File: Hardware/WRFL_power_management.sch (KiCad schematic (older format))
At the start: 38 parts, among them P1 JST_XH_2, P2 TEST_POINT, P3 TEST_POINT, P4 JST_XH_2, P5 TEST_POINT, P6 TEST_POINT, P7 TEST_POINT, Q1 SI1012CR, Q2 SI2333DDS, U1 TPS73633DCQ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

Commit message: Added VREF and 2x3 for servos
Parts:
- R6: value 100k -> 1M
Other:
- moved on the sheet: C6, C7, C8, C9, D2, L1, P7, R8, R9, U4

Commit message: Added VBAT sens
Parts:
- added P17: 1x2_2_54_MALE, symbol CONN_2
- added Q4: SI1012CR, SC-75A, symbol SI1012CR
- added R19, R20: 9.09k_0.1%, ~, symbol R
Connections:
- net labels added: MEAS_EN, VBAT_SENS
- wire segments 96 -> 105
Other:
- note added: "Power on switch + User switch\nUsing the rotary encoder's push button"
- moved on the sheet: R14, R15
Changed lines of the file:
@@
-EESchema Schematic File Version 2  date 10/7/2013 7:37:21 AM
+EESchema Schematic File Version 2  date Monday, October 07, 2013 09:14:17 AM
 LIBS:power
 LIBS:device
@@
 Wire Wire Line
 	6200 1900 6200 2050
-Wire Wire Line
-	6200 2050 7250 2050
-Connection ~ 6750 2050
-$Comp
-L GND #PWR21
+$Comp
+L GND #PWR22
 U 1 1 524B2F1B
 P 6750 3650
-F 0 "#PWR21" H 6750 3650 30  0001 C CNN
+F 0 "#PWR22" H 6750 3650 30  0001 C CNN
 F 1 "GND" H 6750 3580 30  0001 C CNN
 F 2 "" H 6750 3650 60  0000 C CNN
@@
 $EndComp
 $Comp
-L GND #PWR19
+L GND #PWR20
 U 1 1 524B2F2A
 P 6050 3650
-F 0 "#PWR19" H 6050 3650 30  0001 C CNN
+F 0 "#PWR20" H 6050 3650 30  0001 C CNN
 F 1 "GND" H 6050 3580 30  0001 C CNN
 F 2 "" H 6050 3650 60  0000 C CNN
@@
 	3600 6600 3600 6800
 Wire Wire Line
-	3200 6450 4700 6450
+	3200 6450 5400 6450
 Wire Wire Line
 	4150 6450 4150 6800
@@
 Wire Wire Line
 	6950 1300 7700 1300
-Text GLabel 10500 2050 2    60   Input ~ 0
+Text GLabel 10550 3550 2    60   Input ~ 0
 PM_ENABLE
 Wire Wire Line
-	9400 2050 10500 2050
-Text Label 9950 2050 0    60   ~ 0
+	9650 3550 10550 3550
+Text Label 10000 3550 0    60   ~ 0
 PM_EN
 $Comp
@@
 	8550 5950 8550 6000
 $Comp
-L GND #PWR22
+L GND #PWR23
 U 1 1 5251B5EF
 P 8550 6000
-F 0 "#PWR22" H 8550 6000 30  0001 C CNN
+F 0 "#PWR23" H 8550 6000 30  0001 C CNN
 F 1 "GND" H 8550 5930 30  0001 C CNN
 F 2 "" H 8550 6000 60  0000 C CNN
@@
 $EndComp
 $Comp
-L GND #PWR20
+L GND #PWR21
 U 1 1 5251B5FE
 P 6650 5900
-F 0 "#PWR20" H 6650 5900 30  0001 C CNN
+F 0 "#PWR21" H 6650 5900 30  0001 C CNN
 F 1 "GND" H 6650 5830 30  0001 C CNN
 F 2 "" H 6650 5900 60  0000 C CNN
@@
 $EndComp
 $Comp
-L GND #PWR25
+L GND #PWR26
 U 1 1 5251B60D
 P 10050 6150
-F 0 "#PWR25" H 10050 6150 30  0001 C CNN
+F 0 "#PWR26" H 10050 6150 30  0001 C CNN
 F 1 "GND" H 10050 6080 30  0001 C CNN
 F 2 "" H 10050 6150 60  0000 C CNN
@@
 $EndComp
 $Comp
-L GND #PWR23
+L GND #PWR24
 U 1 1 5251B61C
 P 9250 6900
-F 0 "#PWR23" H 9250 6900 30  0001 C CNN
+F 0 "#PWR24" H 9250 6900 30  0001 C CNN
 F 1 "GND" H 9250 6830 30  0001 C CNN
 F 2 "" H 9250 6900 60  0000 C CNN
@@
 	7300 6150 6500 6150
 $Comp
-L V_BOOST #U9
+L V_BOOST #U10
 U 1 1 5251BF9B
 P 10550 5000
-F 0 "#U9" H 10550 5200 60  0001 C CNN
+F 0 "#U10" H 10550 5200 60  0001 C CNN
 F 1 "V_BOOST" H 10550 5100 60  0000 C CNN
 F 2 "~" H 10550 5000 60  0000 C CNN
@@
 $EndComp
 $Comp
-L GND #PWR18
+L GND #PWR19
 U 1 1 5251E6D3
 P 5700 2000
-F 0 "#PWR18" H 5700 2000 30  0001 C CNN
+F 0 "#PWR19" H 5700 2000 30  0001 C CNN
 F 1 "GND" H 5700 1930 30  0001 C CNN
 F 2 "" H 5700 2000 60  0000 C CNN
@@
 Wire Wire Line
 	5700 1800 5700 2000
-Text GLabel 7250 2050 2    60   Input ~ 0
+Text GLabel 7450 3550 2    60   Input ~ 0
 ON_SW_FET
 $Comp
 L R R15
 U 1 1 52521245
-P 9800 2450
-F 0 "R15" V 9880 2450 40  0000 C CNN
-F 1 "100k" V 9807 2451 40  0000 C CNN
-F 2 "~" V 9730 2450 30  0000 C CNN
-F 3 "~" H 9800 2450 30  0000 C CNN
-	1    9800 2450
-	1    0    0    -1
-$EndComp
-$Comp
-L GND #PWR24
+P 9850 3950
+F 0 "R15" V 9930 3950 40  0000 C CNN
+F 1 "100k" V 9857 3951 40  0000 C CNN
+F 2 "~" V 9780 3950 30  0000 C CNN
+F 3 "~" H 9850 3950 30  0000 C CNN
+	1    9850 3950
+	1    0    0    -1
+$EndComp
+$Comp
+L GND #PWR25
 U 1 1 5252124B
-P 9800 2900
-F 0 "#PWR24" H 9800 2900 30  0001 C CNN
-F 1 "GND" H 9800 2830 30  0001 C CNN
-F 2 "" H 9800 2900 60  0000 C CNN
-F 3 "" H 9800 2900 60  0000 C CNN
-	1    9800 2900
-	1    0    0    -1
-$EndComp
-Wire Wire Line
-	9800 2200 9800 2050
-Connection ~ 9800 2050
-Wire Wire Line
-	9800 2700 9800 2900
+P 9850 4400
+F 0 "#PWR25" H 9850 4400 30  0001 C CNN
+F 1 "GND" H 9850 4330 30  0001 C CNN
+F 2 "" H 9850 4400 60  0000 C CNN
+F 3 "" H 9850 4400 60  0000 C CNN
+	1    9850 4400
+	1    0    0    -1
+$EndComp
+Wire Wire Line
+	9850 3700 9850 3550
+Connection ~ 9850 3550
+Wire Wire Line
+	9850 4200 9850 4400
 $Comp
 L R R14
 U 1 1 5252135F
-P 9150 2050
-F 0 "R14" V 9230 2050 40  0000 C CNN
-F 1 "10k" V 9157 2051 40  0000 C CNN
-F 2 "~" V 9080 2050 30  0000 C CNN
-F 3 "~" H 9150 2050 30  0000 C CNN
-	1    9150 2050
+P 9400 3550
+F 0 "R14" V 9480 3550 40  0000 C CNN
+F 1 "10k" V 9407 3551 40  0000 C CNN
+F 2 "~" V 9330 3550 30  0000 C CNN
+F 3 "~" H 9400 3550 30  0000 C CNN
+	1    9400 3550
 	0    -1   -1   0
 $EndComp
-Text GLabel 8650 2050 0    60   Input ~ 0
+Text GLabel 8950 3550 0    60   Input ~ 0
 ON_SW_MCU
 Wire Wire Line
-	8900 2050 8650 2050
+	9150 3550 8950 3550
 Wire Notes Line
-	7650 1900 7800 1900
+	7850 3400 8000 3400
 Wire Notes Line
-	8050 1900 8250 1900
+	8250 3400 8450 3400
 Wire Notes Line
-	7800 1900 8050 1800
+	8000 3400 8250 3300
+$Comp
+L R R19
+U 1 1 5252599E
+P 10500 1600
+F 0 "R19" V 10580 1600 40  0000 C CNN
+F 1 "9.09k_0.1%" V 10400 1600 40  0000 C CNN
+F 2 "~" V 10430 1600 30  0000 C CNN
+F 3 "~" H 10500 1600 30  0000 C CNN
+	1    10500 1600
+	1    0    0    -1
+$EndComp
+Wire Wire Line
+	7300 2050 7300 3550
+Wire Wire Line
+	7300 3550 7450 3550
+Wire Wire Line
+	6200 2050 7300 2050
+Connection ~ 6750 2050
+Text Notes 7350 3150 0    60   ~ 0
+Power on switch + User switch\nUsing the rotary encoder's push button
+$Comp
+L VBAT_SW #U9
+U 1 1 52525B52
+P 10500 950
+F 0 "#U9" H 10500 1150 60  0001 C CNN
+F 1 "VBAT_SW" H 10500 1050 60  0000 C CNN
+F 2 "~" H 10500 950 60  0000 C CNN
+F 3 "~" H 10500 950 60  0000 C CNN
+	1    10500 950
+	1    0    0    -1
+$EndComp
+$Comp
+L R R20
+U 1 1 52525B62
+P 10500 2250
+F 0 "R20" V 10580 2250 40  0000 C CNN
+F 1 "9.09k_0.1%" V 10400 2250 40  0000 C CNN
+F 2 "~" V 10430 2250 30  0000 C CNN
+F 3 "~" H 10500 2250 30  0000 C CNN
+	1    10500 2250
+	1    0    0    -1
+$EndComp
+$Comp
+L SI1012CR Q4
+U 1 1 52525B68
+P 10400 2850
+F 0 "Q4" H 10600 2850 60  0000 C CNN
+F 1 "SI1012CR" H 10750 2750 60  0000 C CNN
+F 2 "SC-75A" H 10400 2850 60  0001 C CNN
+F 3 "http://www.vishay.com/docs/67519/si1012cr.pdf" H 10350 2600 60  0001 C CNN
+	1    10400 2850
+	1    0    0    -1
+$EndComp
+$Comp
+L GND #PWR27
+U 1 1 52525B6E
+P 10500 3200
+F 0 "#PWR27" H 10500 3200 30  0001 C CNN
+F 1 "GND" H 10500 3130 30  0001 C CNN
+F 2 "" H 10500 3200 60  0000 C CNN
+F 3 "" H 10500 3200 60  0000 C CNN
+	1    10500 3200
+	1    0    0    -1
+$EndComp
+Wire Wire Line
+	10500 1150 10500 1350
+Wire Wire Line
+	10500 1850 10500 2000
+Wire Wire Line
+	10500 2500 10500 2650
+Wire Wire Line
+	10500 3050 10500 3200
+Text GLabel 9650 2850 0    60   Input ~ 0
+MEAS_EN
+Wire Wire Line
+	9650 2850 10200 2850
+Text GLabel 9650 1950 0    60   Input ~ 0
+VBAT_SENS
+Wire Wire Line
+	9650 1950 10500 1950
+Connection ~ 10500 1950
+$Comp
+L CONN_2 P17
+U 1 1 52526A5A
+P 5750 6550
+F 0 "P17" H 5700 6750 40  0000 C CNN
+F 1 "1x2_2_54_MALE" H 5800 6350 40  0000 C CNN
+F 2 "" H 5750 6550 60  0000 C CNN
+F 3 "" H 5750 6550 60  0000 C CNN
+	1    5750 6550
+	1    0    0    -1
+$EndComp
+$Comp
+L GND #PWR18
+U 1 1 52526A67
+P 5400 7250
+F 0 "#PWR18" H 5400 7250 30  0001 C CNN
+F 1 "GND" H 5400 7180 30  0001 C CNN
+F 2 "" H 5400 7250 60  0000 C CNN
+F 3 "" H 5400 7250 60  0000 C CNN
+	1    5400 7250
+	1    0    0    -1
+$EndComp
+Wire Wire Line
+	5400 6650 5400 7250
 $EndSCHEMATC

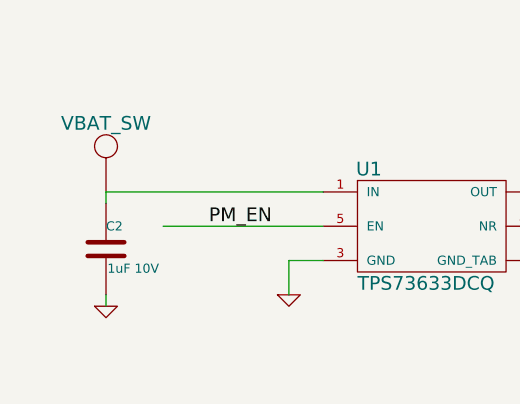
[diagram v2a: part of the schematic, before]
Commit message: added footprint values for caps and resistors
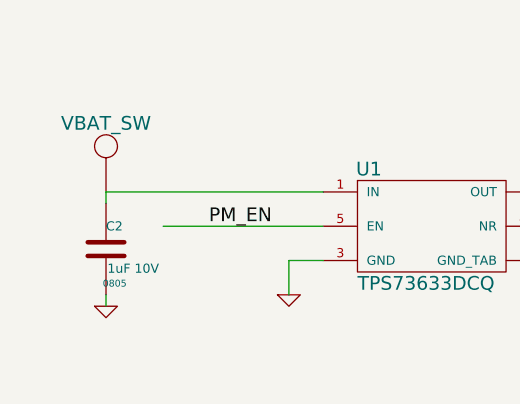
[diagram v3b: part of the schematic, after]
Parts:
- C1, C15, C16, C2, C3, C4, C5, C6, C7, C8, C9, R1, R14, R15, R19, R2, R20, R3, R4, R5, R6, R7, R8, R9: footprint ~ -> 0805
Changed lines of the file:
@@
-EESchema Schematic File Version 2  date Monday, October 07, 2013 09:14:17 AM
+EESchema Schematic File Version 2  date Monday, October 07, 2013 12:52:48 PM
 LIBS:power
 LIBS:device
@@
 F 0 "R7" V 6280 1650 40  0000 C CNN
 F 1 "1M" V 6207 1651 40  0000 C CNN
-F 2 "~" V 6130 1650 30  0000 C CNN
+F 2 "0805" V 6130 1650 30  0001 C CNN
 F 3 "~" H 6200 1650 30  0000 C CNN
 	1    6200 1650
@@
 F 0 "R6" V 6130 3300 40  0000 C CNN
 F 1 "1M" V 6057 3301 40  0000 C CNN
-F 2 "~" V 5980 3300 30  0000 C CNN
+F 2 "0805" V 5980 3300 30  0001 C CNN
 F 3 "~" H 6050 3300 30  0000 C CNN
 	1    6050 3300
@@
 F 0 "R1" V 1380 1850 40  0000 C CNN
 F 1 "9.09k_0.1%" V 1200 1850 40  0000 C CNN
-F 2 "~" V 1230 1850 30  0000 C CNN
+F 2 "0805" V 1230 1850 30  0001 C CNN
 F 3 "~" H 1300 1850 30  0000 C CNN
 	1    1300 1850
@@
 F 0 "R2" V 1380 3150 40  0000 C CNN
 F 1 "9.09k_0.1%" V 1200 3150 40  0000 C CNN
-F 2 "~" V 1230 3150 30  0000 C CNN
+F 2 "0805" V 1230 3150 30  0001 C CNN
 F 3 "~" H 1300 3150 30  0000 C CNN
 	1    1300 3150
@@
 F 0 "C1" H 1300 5100 40  0000 L CNN
 F 1 "1uF 10V" H 1306 4915 40  0000 L CNN
-F 2 "~" H 1338 4850 30  0000 C CNN
+F 2 "0805" H 1338 4850 30  0001 C CNN
 F 3 "~" H 1300 5000 60  0000 C CNN
 	1    1300 5000
@@
 F 0 "C4" H 3700 5100 40  0000 L CNN
 F 1 "1uF 10V" H 3706 4915 40  0000 L CNN
-F 2 "~" H 3738 4850 30  0000 C CNN
+F 2 "0805" H 3738 4850 30  0001 C CNN
 F 3 "~" H 3700 5000 60  0000 C CNN
 	1    3700 5000
@@
 F 0 "C3" H 3600 7100 40  0000 L CNN
 F 1 "0.01uF 25V" H 3606 6915 40  0000 L CNN
-F 2 "~" H 3638 6850 30  0000 C CNN
+F 2 "0805" H 3638 6850 30  0001 C CNN
 F 3 "~" H 3600 7000 60  0000 C CNN
 	1    3600 7000
@@
 F 0 "C2" H 1300 6800 40  0000 L CNN
 F 1 "1uF 10V" H 1306 6615 40  0000 L CNN
-F 2 "~" H 1338 6550 30  0000 C CNN
+F 2 "0805" H 1338 6550 30  0000 C CNN
 F 3 "~" H 1300 6700 60  0000 C CNN
 	1    1300 6700
@@
 F 0 "C5" H 4150 7100 40  0000 L CNN
 F 1 "1uF 10V" H 4156 6915 40  0000 L CNN
-F 2 "~" H 4188 6850 30  0000 C CNN
+F 2 "0805" H 4188 6850 30  0001 C CNN
 F 3 "~" H 4150 7000 60  0000 C CNN
 	1    4150 7000
@@
 F 0 "C9" H 10050 5900 40  0000 L CNN
 F 1 "10uF 16V" H 10056 5715 40  0000 L CNN
-F 2 "~" H 10088 5650 30  0000 C CNN
+F 2 "0805" H 10088 5650 30  0001 C CNN
 F 3 "~" H 10050 5800 60  0000 C CNN
 	1    10050 5800
@@
 F 0 "C8" H 9550 5900 40  0000 L CNN
 F 1 "680pF" H 9556 5715 40  0000 L CNN
-F 2 "~" H 9588 5650 30  0000 C CNN
+F 2 "0805" H 9588 5650 30  0001 C CNN
 F 3 "~" H 9550 5800 60  0000 C CNN
 	1    9550 5800
@@
 F 0 "R9" V 9330 6550 40  0000 C CNN
 F 1 "10k" V 9257 6551 40  0000 C CNN
-F 2 "~" V 9180 6550 30  0000 C CNN
+F 2 "0805" V 9180 6550 30  0001 C CNN
 F 3 "~" H 9250 6550 30  0000 C CNN
 	1    9250 6550
@@
 F 0 "R8" V 9330 5850 40  0000 C CNN
 F 1 "31.6k" V 9257 5851 40  0000 C CNN
-F 2 "~" V 9180 5850 30  0000 C CNN
+F 2 "0805" V 9180 5850 30  0001 C CNN
 F 3 "~" H 9250 5850 30  0000 C CNN
 	1    9250 5850
@@
 F 0 "R4" V 2280 2050 40  0000 C CNN
 F 1 "2k" V 2207 2051 40  0000 C CNN
-F 2 "~" V 2130 2050 30  0000 C CNN
+F 2 "0805" V 2130 2050 30  0001 C CNN
 F 3 "~" H 2200 2050 30  0000 C CNN
 	1    2200 2050
@@
 F 0 "R3" V 1930 2050 40  0000 C CNN
 F 1 "825" V 1857 2051 40  0000 C CNN
-F 2 "~" V 1780 2050 30  0000 C CNN
+F 2 "0805" V 1780 2050 30  0001 C CNN
 F 3 "~" H 1850 2050 30  0000 C CNN
 	1    1850 2050
@@
 F 0 "R5" V 5330 2000 40  0000 C CNN
 F 1 "100k" V 5257 2001 40  0000 C CNN
-F 2 "~" V 5180 2000 30  0000 C CNN
+F 2 "0805" V 5180 2000 30  0001 C CNN
 F 3 "~" H 5250 2000 30  0000 C CNN
 	1    5250 2000
@@
 F 0 "C7" H 6650 5700 40  0000 L CNN
 F 1 "10uF 16V" H 6656 5515 40  0000 L CNN
-F 2 "~" H 6688 5450 30  0000 C CNN
+F 2 "0805" H 6688 5450 30  0001 C CNN
 F 3 "~" H 6650 5600 60  0000 C CNN
 	1    6650 5600
@@
 F 0 "C6" H 6350 5700 40  0000 L CNN
 F 1 "10uF 16V" H 6356 5515 40  0000 L CNN
-F 2 "~" H 6388 5450 30  0000 C CNN
+F 2 "0805" H 6388 5450 30  0001 C CNN
 F 3 "~" H 6350 5600 60  0000 C CNN
 	1    6350 5600
@@
 F 0 "C15" H 1550 1950 40  0000 L CNN
 F 1 "10uF 16V" H 1556 1765 40  0000 L CNN
-F 2 "~" H 1588 1700 30  0000 C CNN
+F 2 "0805" H 1588 1700 30  0001 C CNN
 F 3 "~" H 1550 1850 60  0000 C CNN
 	1    1550 1850
@@
 F 0 "C16" H 5700 1700 40  0000 L CNN
 F 1 "10uF 16V" H 5706 1515 40  0000 L CNN
-F 2 "~" H 5738 1450 30  0000 C CNN
+F 2 "0805" H 5738 1450 30  0001 C CNN
 F 3 "~" H 5700 1600 60  0000 C CNN
 	1    5700 1600
@@
 F 0 "R15" V 9930 3950 40  0000 C CNN
 F 1 "100k" V 9857 3951 40  0000 C CNN
-F 2 "~" V 9780 3950 30  0000 C CNN
+F 2 "0805" V 9780 3950 30  0001 C CNN
 F 3 "~" H 9850 3950 30  0000 C CNN
 	1    9850 3950
@@
 F 0 "R14" V 9480 3550 40  0000 C CNN
 F 1 "10k" V 9407 3551 40  0000 C CNN
-F 2 "~" V 9330 3550 30  0000 C CNN
+F 2 "0805" V 9330 3550 30  0001 C CNN
 F 3 "~" H 9400 3550 30  0000 C CNN
 	1    9400 3550
@@
 F 0 "R19" V 10580 1600 40  0000 C CNN
 F 1 "9.09k_0.1%" V 10400 1600 40  0000 C CNN
-F 2 "~" V 10430 1600 30  0000 C CNN
+F 2 "0805" V 10430 1600 30  0001 C CNN
 F 3 "~" H 10500 1600 30  0000 C CNN
 	1    10500 1600
@@
 F 0 "R20" V 10580 2250 40  0000 C CNN
 F 1 "9.09k_0.1%" V 10400 2250 40  0000 C CNN
-F 2 "~" V 10430 2250 30  0000 C CNN
+F 2 "0805" V 10430 2250 30  0001 C CNN
 F 3 "~" H 10500 2250 30  0000 C CNN
 	1    10500 2250

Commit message: Schematics update
Bluetooth sheet added
LCD specific symbol
power management sheet rearrangement
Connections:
- wire segments 105 -> 104
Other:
- note added: "BAT NTC"
- note added: "Battery"
- moved on the sheet: C1, C15, C2, C3, C4, C5, C6, C7, C8, C9, D2, L1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

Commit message: more changes
Changed BAS40 to BAT54C
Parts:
- removed D1: BAS40-05-V, symbol BAS40-05-V
- added D1: BAT54C-V, SOT-23, symbol BAT54C-V
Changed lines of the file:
@@
-EESchema Schematic File Version 2  date 10/11/2013 1:57:23 AM
+EESchema Schematic File Version 2  date Tuesday, October 15, 2013 09:37:22 AM
 LIBS:power
 LIBS:device
@@
 Sheet 2 6
 Title "WRFL power management"
-Date "10 oct 2013"
+Date "15 oct 2013"
 Rev "1.0"
 Comp "Nightmechanic"
@@
 Wire Wire Line
 	1300 2300 1300 2900
-$Comp
-L BAS40-05-V D1
-U 1 1 524B3606
-P 5100 2900
-F 0 "D1" H 5050 3150 60  0000 C CNN
-F 1 "BAS40-05-V" H 5100 2700 60  0000 C CNN
-F 2 "" H 5100 2900 60  0000 C CNN
-F 3 "http://www.vishay.com/docs/85701/bas40v.pdf" H 5050 2600 60  0001 C CNN
-	1    5100 2900
-	1    0    0    -1
-$EndComp
 Connection ~ 6050 2900
 Wire Wire Line
@@
 	1050 6650 1050 6550
 Connection ~ 1050 6550
+$Comp
+L BAT54C-V D1
+U 1 1 525D7621
+P 5100 2900
+F 0 "D1" H 5050 3150 60  0000 C CNN
+F 1 "BAT54C-V" H 5100 2700 60  0000 C CNN
+F 2 "SOT-23" H 5100 2900 60  0001 C CNN
+F 3 "http://www.vishay.com/docs/85508/bat54v.pdf" H 5050 2600 60  0001 C CNN
+	1    5100 2900
+	1    0    0    -1
+$EndComp
 $EndSCHEMATC

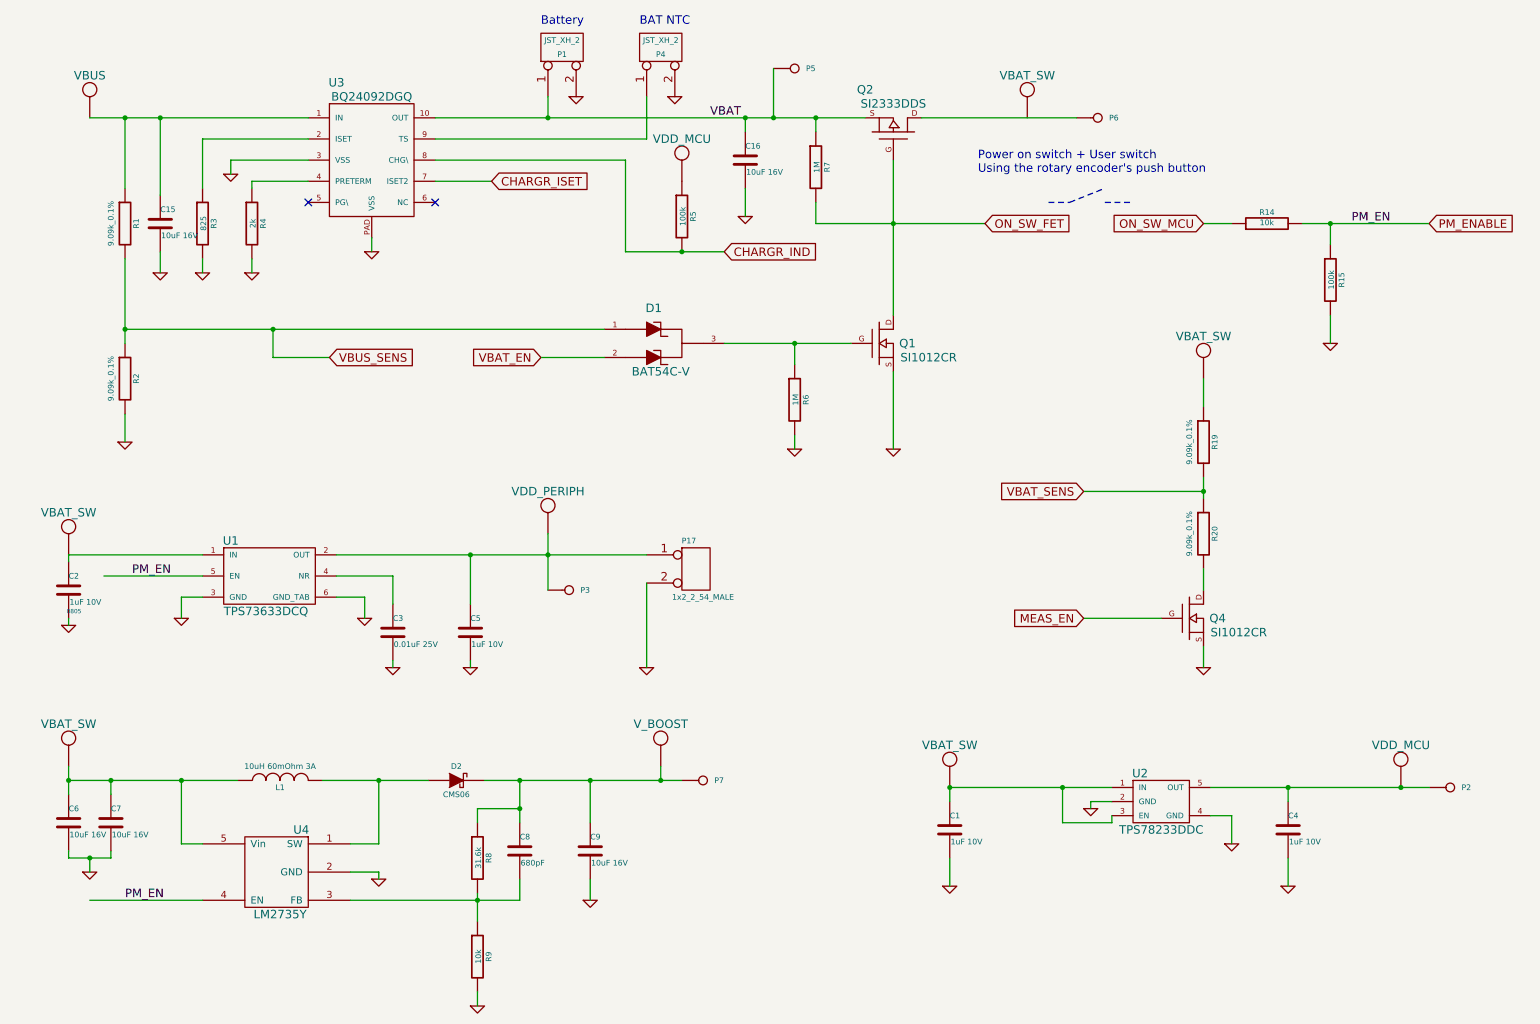
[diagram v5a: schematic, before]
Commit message: MCU function assignment
BT RTS/CTS as test points,
BT reset GPIO option
Launchpad header pin function assignment (for ERC check)
Power symbols corrections
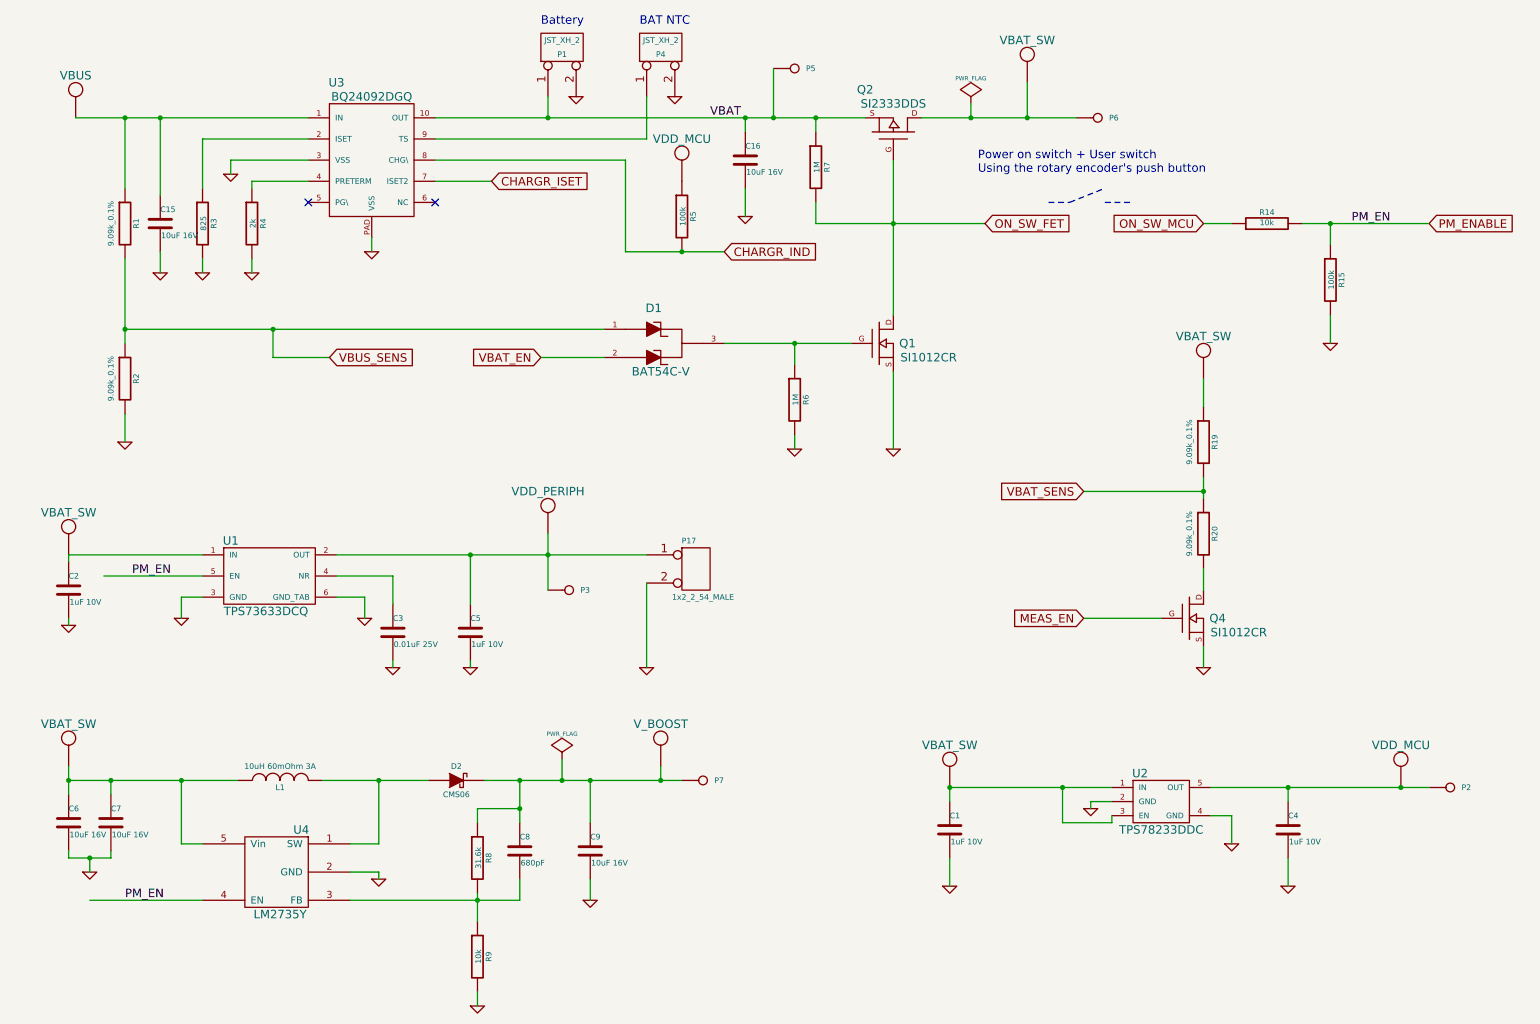
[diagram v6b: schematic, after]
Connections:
- net VBAT_SW: now also P6.1, Q2.D
